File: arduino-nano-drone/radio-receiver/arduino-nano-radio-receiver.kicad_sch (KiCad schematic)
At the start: 8 parts, among them J1 Conn_01x04_Pin, J2 Conn_01x04_Pin, J3 Conn_01x04_Pin, U2 AMS1117-3.3, U3 NRF24L01_Breakout

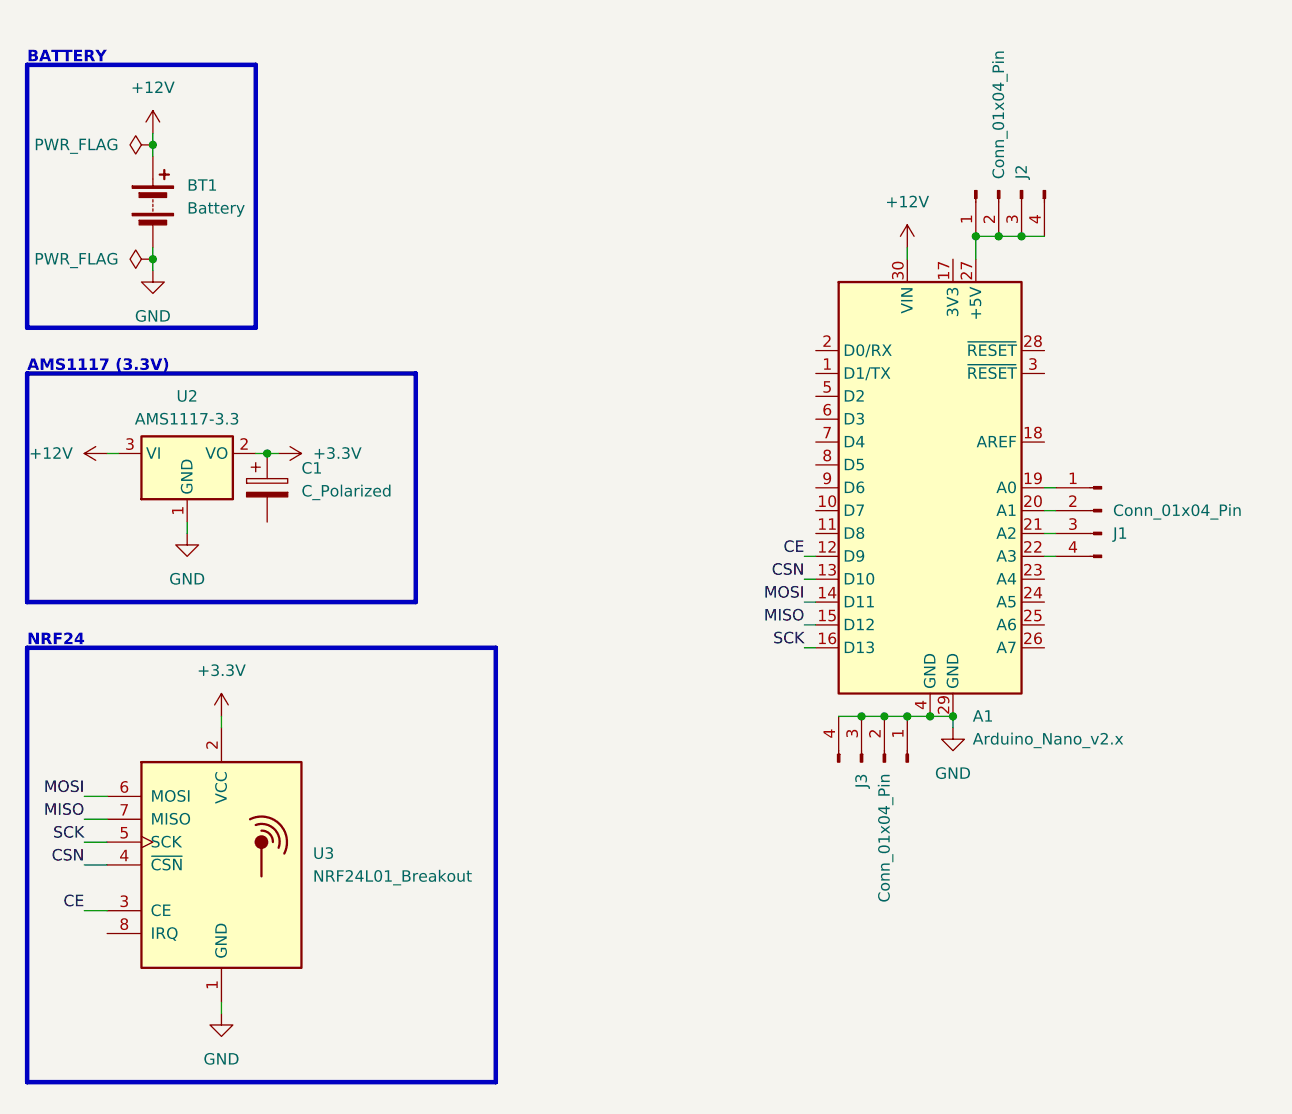
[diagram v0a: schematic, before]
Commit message: project 8 / arduino nano drone / added radio transmitter and improved schematics
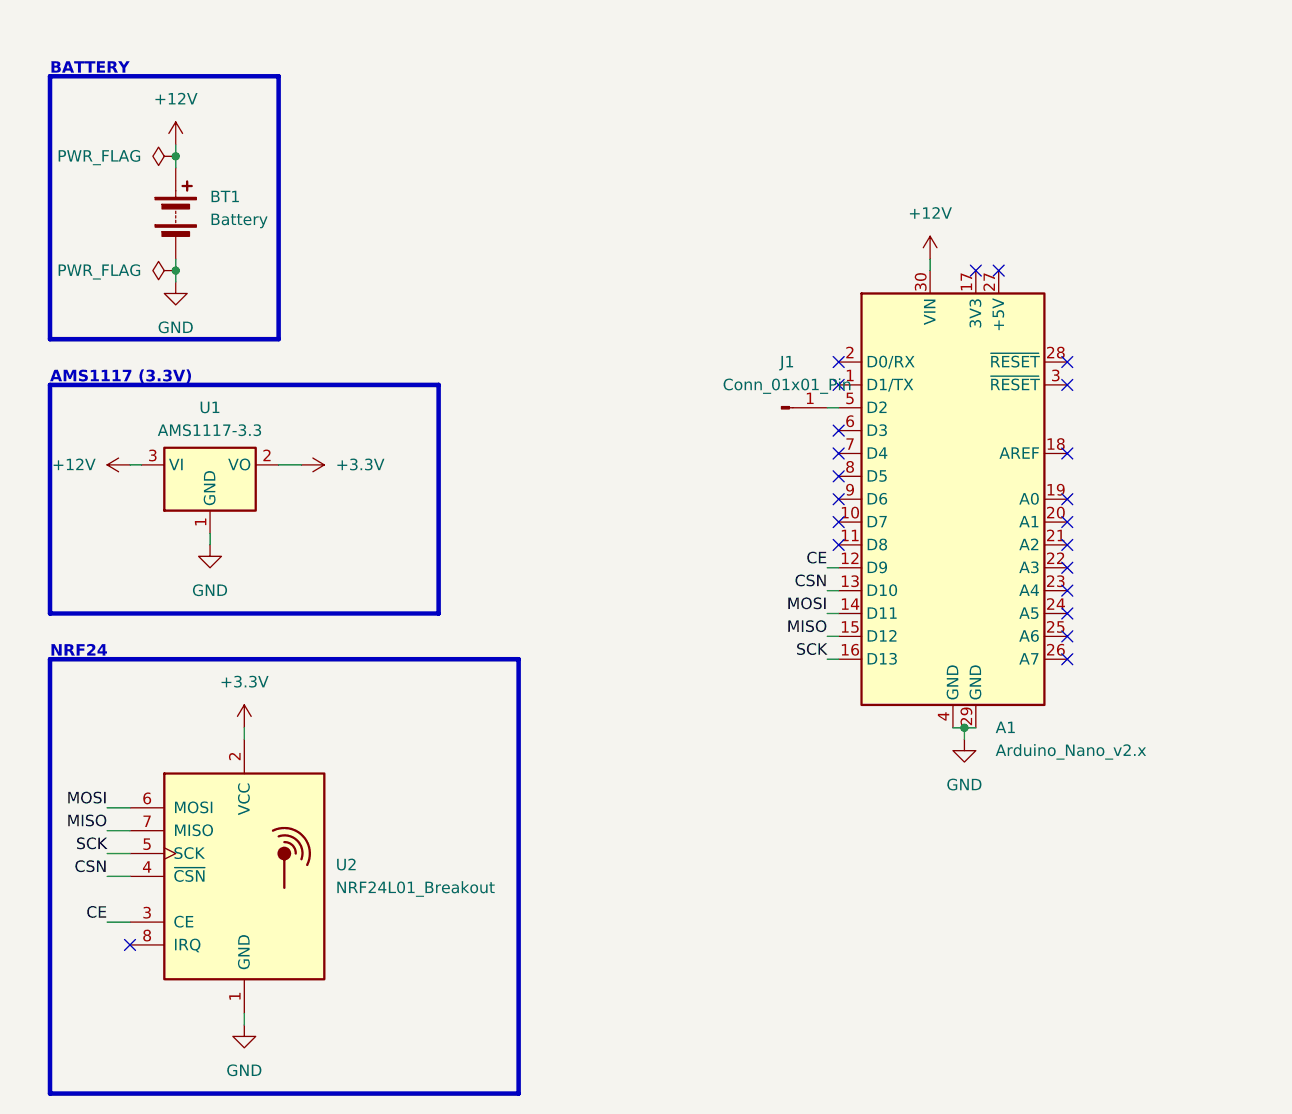
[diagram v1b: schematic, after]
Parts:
- removed C1: C_Polarized, symbol Device:C_Polarized
- removed J1, J2, J3: Conn_01x04_Pin, symbol Connector:Conn_01x04_Pin
- removed U2: AMS1117-3.3, Package_TO_SOT_SMD:SOT-223-3_TabPin2, symbol Regulator_Linear:AMS1117-3.3
- removed U3: NRF24L01_Breakout, RF_Module:nRF24L01_Breakout, symbol RF:NRF24L01_Breakout
- added J1: Conn_01x01_Pin, symbol Connector:Conn_01x01_Pin
- added U1: AMS1117-3.3, Package_TO_SOT_SMD:SOT-223-3_TabPin2, symbol Regulator_Linear:AMS1117-3.3
- added U2: NRF24L01_Breakout, RF_Module:nRF24L01_Breakout, symbol RF:NRF24L01_Breakout
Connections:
- net +12V: now also U1.3 (VI)
- net +3.3V: now also U1.2 (VO), U2.2 (VCC)
- net CE: now also U2.3 (CE)
- net CSN: now also U2.4 (~{CSN})
- net GND: now also U1.1 (GND), U2.1 (GND)
- net MISO: now also U2.7 (MISO)
- net MOSI: now also U2.6 (MOSI)
- net SCK: now also U2.5 (SCK)
- net at A1.5 (D2): now also J1.1 (Pin_1)
- no-connect marks 0 -> 22
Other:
- title: Arduino Nano Radio Transmitter -> Arduino Nano Radio Receiver

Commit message: project 8 / arduino nano drone / added rt, rr, fl pcb, improved layout
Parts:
- BT1: footprint (none) -> Connector_PinHeader_2.54mm:PinHeader_1x02_P2.54mm_Vertical
- J1: footprint (none) -> Connector_PinHeader_2.54mm:PinHeader_1x01_P2.54mm_Vertical
- U1: footprint Package_TO_SOT_SMD:SOT-223-3_TabPin2 -> Connector_PinSocket_2.54mm:PinSocket_1x03_P2.54mm_Vertical
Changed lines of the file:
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@@
       (effects (font (size 1.27 1.27)) (justify left))
     )
-    (property "Footprint" "" (at 30.48 31.496 90)
+    (property "Footprint" "Connector_PinHeader_2.54mm:PinHeader_1x02_P2.54mm_Vertical" (at 30.48 31.496 90)
       (effects (font (size 1.27 1.27)) hide)
     )
@@
       (effects (font (size 1.27 1.27)))
     )
-    (property "Footprint" "Package_TO_SOT_SMD:SOT-223-3_TabPin2" (at 34.29 55.88 0)
+    (property "Footprint" "Connector_PinSocket_2.54mm:PinSocket_1x03_P2.54mm_Vertical" (at 34.29 55.88 0)
       (effects (font (size 1.27 1.27)) hide)
     )
@@
       (effects (font (size 1.27 1.27)))
     )
-    (property "Footprint" "" (at 97.79 54.61 0)
-      (effects (font (size 1.27 1.27)) hide)
-    )
+    (property "Footprint" "Connector_PinHeader_2.54mm:PinHeader_1x01_P2.54mm_Vertical" (at 97.79 54.61 0)
+      (effects (font (size 1.27 1.27)) hide)
+    )

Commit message: Reviewed schematics and boards
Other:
- note added: "Uwagi jak w transmiterze"
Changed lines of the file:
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@@
     (effects (font (size 1.27 1.27) (thickness 0.254) bold (color 0 0 0 1)) (justify left bottom))
+  )
+  (text "Uwagi jak w transmiterze" (at 62.23 64.77 0)
+    (effects (font (size 3 3) (thickness 0.6) bold (color 255 0 47 1)) (justify left bottom))
   )
   (text "NRF24" (at 16.51 82.55 0)

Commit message: project 8 / arduino nano drone / improved schematics, pcb after review
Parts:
- added C1, C2: 10u, Capacitor_THT:CP_Radial_D4.0mm_P1.50mm, symbol Device:C_Polarized
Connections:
- net +3.3V: now also C1.1, C2.1
- net GND: now also C1.2, C2.2
- net IRQ: now reaches A1.11 (D8)
- net IRQ: now also U2.8 (IRQ)
- no-connect marks 22 -> 20
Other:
- note removed: "Uwagi jak w transmiterze"
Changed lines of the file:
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@@
     (comment 1 "N/A")
+  )
+  (junction (at 43.18 60.96) (diameter 0) (color 0 0 0 0)
+  )
+  (junction (at 38.1 90.17) (diameter 0) (color 0 0 0 0)
   )
   (junction (at 30.48 26.67) (diameter 0) (color 0 0 0 0)
@@
   (no_connect (at 129.54 67.31))
   (no_connect (at 129.54 64.77))
-  (no_connect (at 25.4 114.3))
   (no_connect (at 119.38 39.37))
   (no_connect (at 129.54 74.93))
@@
   (no_connect (at 129.54 72.39))
   (no_connect (at 104.14 62.23))
-  (no_connect (at 104.14 69.85))
   (no_connect (at 104.14 64.77))
   (no_connect (at 129.54 59.69))
@@
     (stroke (width 0) (type default))
   )
+  (wire (pts (xy 38.1 90.17) (xy 38.1 91.44))
+    (stroke (width 0) (type default))
+  )
   (wire (pts (xy 30.48 26.67) (xy 30.48 27.94))
     (stroke (width 0) (type default))
   )
+  (wire (pts (xy 48.26 90.17) (xy 49.53 90.17))
+    (stroke (width 0) (type default))
+  )
+  (wire (pts (xy 43.18 60.96) (xy 44.45 60.96))
+    (stroke (width 0) (type default))
+  )
+  (wire (pts (xy 102.87 69.85) (xy 104.14 69.85))
+    (stroke (width 0) (type default))
+  )
   (wire (pts (xy 30.48 25.4) (xy 30.48 26.67))
     (stroke (width 0) (type default))
   )
+  (wire (pts (xy 38.1 90.17) (xy 40.64 90.17))
+    (stroke (width 0) (type default))
+  )
   (wire (pts (xy 118.11 90.17) (xy 119.38 90.17))
     (stroke (width 0) (type default))
   )
-  (wire (pts (xy 41.91 60.96) (xy 44.45 60.96))
+  (wire (pts (xy 41.91 60.96) (xy 43.18 60.96))
     (stroke (width 0) (type default))
   )
@@
     (stroke (width 0) (type default))
   )
-  (wire (pts (xy 38.1 90.17) (xy 38.1 91.44))
+  (wire (pts (xy 38.1 88.9) (xy 38.1 90.17))
     (stroke (width 0) (type default))
   )
@@
     (stroke (width 0) (type default))
   )
+  (wire (pts (xy 22.86 114.3) (xy 25.4 114.3))
+    (stroke (width 0) (type default))
+  )
   (wire (pts (xy 102.87 74.93) (xy 104.14 74.93))
     (stroke (width 0) (type default))
@@
     (stroke (width 0) (type default))
   )
+  (wire (pts (xy 43.18 69.85) (xy 43.18 68.58))
+    (stroke (width 0) (type default))
+  )
   (wire (pts (xy 114.3 38.1) (xy 114.3 39.37))
+    (stroke (width 0) (type default))
+  )
+  (wire (pts (xy 49.53 90.17) (xy 49.53 91.44))
     (stroke (width 0) (type default))
   )
@@
     (effects (font (size 1.27 1.27) (thickness 0.254) bold (color 0 0 0 1)) (justify left bottom))
   )
-  (text "Uwagi jak w transmiterze" (at 62.23 64.77 0)
-    (effects (font (size 3 3) (thickness 0.6) bold (color 255 0 47 1)) (justify left bottom))
-  )
   (text "NRF24" (at 16.51 82.55 0)
     (effects (font (size 1.27 1.27) (thickness 0.254) bold (color 0 0 0 1)) (justify left bottom))
@@
     (effects (font (size 1.27 1.27) (thickness 0.254) bold (color 0 0 0 1)) (justify left bottom))
   )
+  (label "IRQ" (at 102.87 69.85 180) (fields_autoplaced)
+    (effects (font (size 1.27 1.27)) (justify right bottom))
+  )
   (label "SCK" (at 102.87 82.55 180) (fields_autoplaced)
     (effects (font (size 1.27 1.27)) (justify right bottom))
   )
   (label "SCK" (at 22.86 104.14 180) (fields_autoplaced)
+    (effects (font (size 1.27 1.27)) (justify right bottom))
+  )
+  (label "IRQ" (at 22.86 114.3 180) (fields_autoplaced)
     (effects (font (size 1.27 1.27)) (justify right bottom))
   )
@@
     )
   )
+  (symbol (lib_id "power:GND") (at 43.18 69.85 0) (unit 1)
+    (in_bom yes) (on_board yes) (dnp no) (fields_autoplaced)
+    (property "Reference" "#PWR011" (at 43.18 76.2 0)
+      (effects (font (size 1.27 1.27)) hide)
+    )
+    (property "Value" "GND" (at 43.18 74.93 0)
+      (effects (font (size 1.27 1.27)))
+    )
+    (property "Footprint" "" (at 43.18 69.85 0)
+      (effects (font (size 1.27 1.27)) hide)
+    )
+    (property "Datasheet" "" (at 43.18 69.85 0)
+      (effects (font (size 1.27 1.27)) hide)
+    )
+    (pin "1")
+    (instances
+      (project "arduino-nano-radio-receiver"
+        (path "/25b61d94-19a7-4430-abc4-0e873b590952"
+          (reference "#PWR011") (unit 1)
+        )
+      )
+      (project "arduino-nano-radio-transmitter"
+        (path "/d9490172-cce4-4de5-848d-de895285794a"
+          (reference "#PWR03") (unit 1)
+        )
+      )
+    )
+  )
   (symbol (lib_id "power:GND") (at 118.11 91.44 0) (unit 1)
     (in_bom yes) (on_board yes) (dnp no) (fields_autoplaced)
@@
     )
   )
-  (symbol (lib_id "power:+3.3V") (at 38.1 90.17 0) (unit 1)
-    (in_bom yes) (on_board yes) (dnp no) (fields_autoplaced)
-    (property "Reference" "#PWR05" (at 38.1 93.98 0)
+  (symbol (lib_id "power:+3.3V") (at 38.1 88.9 0) (unit 1)
+    (in_bom yes) (on_board yes) (dnp no)
+    (property "Reference" "#PWR05" (at 38.1 92.71 0)
       (effects (font (size 1.27 1.27)) hide)
     )
@@
       (effects (font (size 1.27 1.27)))
     )
-    (property "Footprint" "" (at 38.1 90.17 0)
-      (effects (font (size 1.27 1.27)) hide)
-    )
-    (property "Datasheet" "" (at 38.1 90.17 0)
+    (property "Footprint" "" (at 38.1 88.9 0)
+      (effects (font (size 1.27 1.27)) hide)
+    )
+    (property "Datasheet" "" (at 38.1 88.9 0)
       (effects (font (size 1.27 1.27)) hide)
     )
@@
     )
   )
+  (symbol (lib_id "Device:C_Polarized") (at 43.18 64.77 0) (unit 1)
+    (in_bom yes) (on_board yes) (dnp no)
+    (property "Reference" "C2" (at 48.26 68.58 90)
+      (effects (font (size 1.27 1.27)))
+    )
+    (property "Value" "10u" (at 45.72 68.58 90)
+      (effects (font (size 1.27 1.27)))
+    )
+    (property "Footprint" "Capacitor_THT:CP_Radial_D4.0mm_P1.50mm" (at 44.1452 68.58 0)
+      (effects (font (size 1.27 1.27)) hide)
+    )
+    (property "Datasheet" "~" (at 43.18 64.77 0)
+      (effects (font (size 1.27 1.27)) hide)
+    )
+    (pin "1")
+    (pin "2")
+    (instances
+      (project "arduino-nano-radio-receiver"
+        (path "/25b61d94-19a7-4430-abc4-0e873b590952"
+          (reference "C2") (unit 1)
+        )
+      )
+    )
+  )
+  (symbol (lib_id "Device:C_Polarized") (at 44.45 90.17 90) (unit 1)
+    (in_bom yes) (on_board yes) (dnp no)
+    (property "Reference" "C1" (at 48.26 85.09 90)
+      (effects (font (size 1.27 1.27)))
+    )
+    (property "Value" "10u" (at 48.26 87.63 90)
+      (effects (font (size 1.27 1.27)))
+    )
+    (property "Footprint" "Capacitor_THT:CP_Radial_D4.0mm_P1.50mm" (at 48.26 89.2048 0)
+      (effects (font (size 1.27 1.27)) hide)
+    )
+    (property "Datasheet" "~" (at 44.45 90.17 0)
+      (effects (font (size 1.27 1.27)) hide)
+    )
+    (pin "1")
+    (pin "2")
+    (instances
+      (project "arduino-nano-radio-receiver"
+        (path "/25b61d94-19a7-4430-abc4-0e873b590952"
+          (reference "C1") (unit 1)
+        )
+      )
+    )
+  )
   (symbol (lib_id "Connector:Conn_01x01_Pin") (at 97.79 54.61 0) (unit 1)
-    (in_bom yes) (on_board yes) (dnp no) (fields_autoplaced)
+    (in_bom yes) (on_board yes) (dnp no)
     (property "Reference" "J1" (at 98.425 49.53 0)
       (effects (font (size 1.27 1.27)))
     )
-    (property "Value" "Conn_01x01_Pin" (at 98.425 52.07 0)
+    (property "Value" "Conn_01x01_Pin" (at 95.25 52.07 0)
       (effects (font (size 1.27 1.27)))
     )
@@
         )
       )
+    )
+  )
+  (symbol (lib_id "power:GND") (at 49.53 91.44 0) (unit 1)
+    (in_bom yes) (on_board yes) (dnp no) (fields_autoplaced)
+    (property "Reference" "#PWR010" (at 49.53 97.79 0)
+      (effects (font (size 1.27 1.27)) hide)
+    )
+    (property "Value" "GND" (at 49.53 96.52 0)
+      (effects (font (size 1.27 1.27)))
+    )
+    (property "Footprint" "" (at 49.53 91.44 0)
+      (effects (font (size 1.27 1.27)) hide)
+    )
+    (property "Datasheet" "" (at 49.53 91.44 0)
+      (effects (font (size 1.27 1.27)) hide)
+    )
+    (pin "1")
+    (instances
+      (project "arduino-nano-radio-receiver"
+        (path "/25b61d94-19a7-4430-abc4-0e873b590952"
+          (reference "#PWR010") (unit 1)
+        )
+      )
+      (project "arduino-nano-radio-transmitter"
+        (path "/d9490172-cce4-4de5-848d-de895285794a"
+          (reference "#PWR03") (unit 1)
+        )
+      )
